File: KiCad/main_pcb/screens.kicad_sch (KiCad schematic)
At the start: 16 parts, among them U4 TI TXB0104DR, U5 ILI9488, U6 TI TXB0104DR, U7 SD Card Socket, U9 TI TXB0104DR

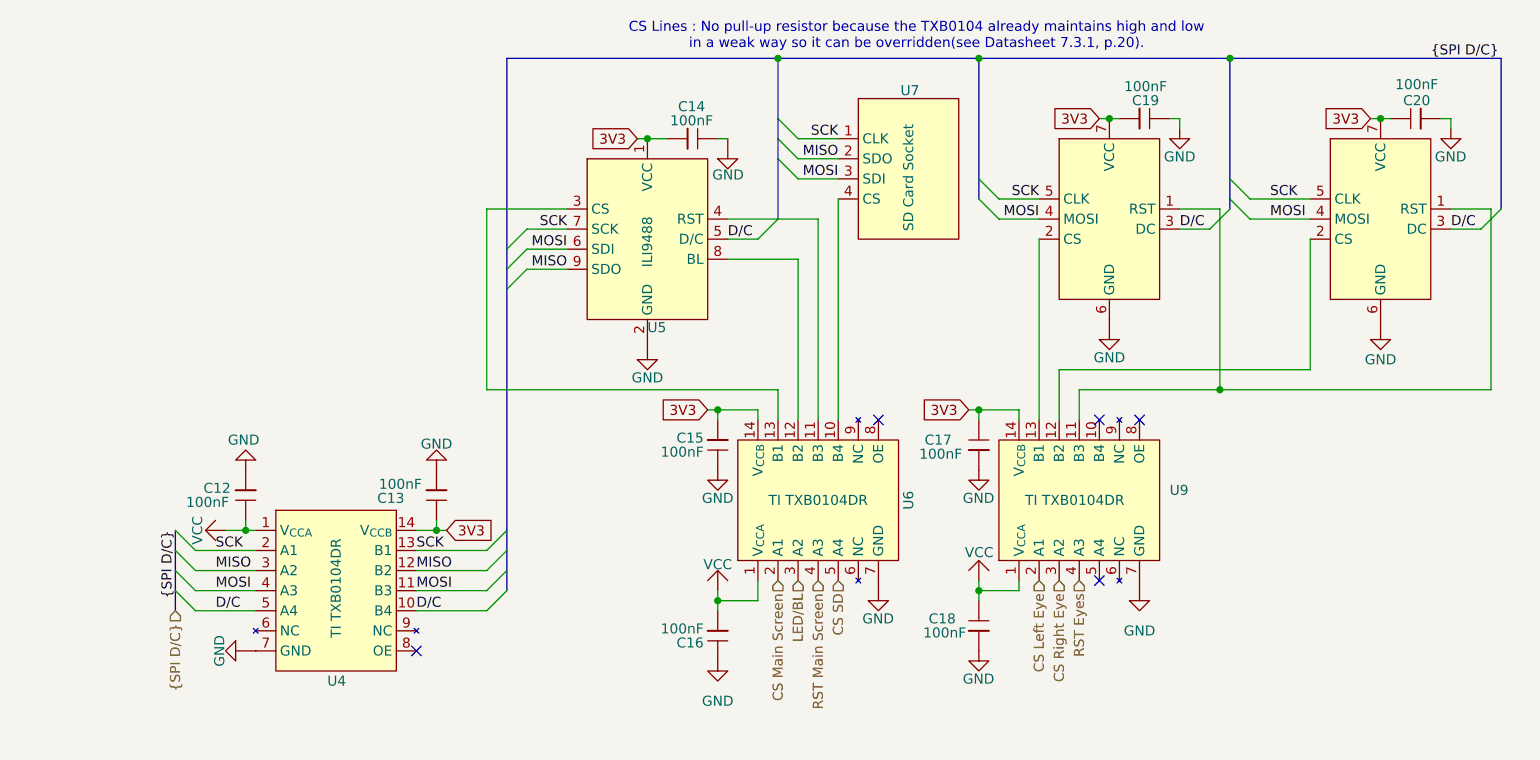
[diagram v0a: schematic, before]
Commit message: feat(schematic): Adds headers instead of direct screens plugging and refactors schematic.
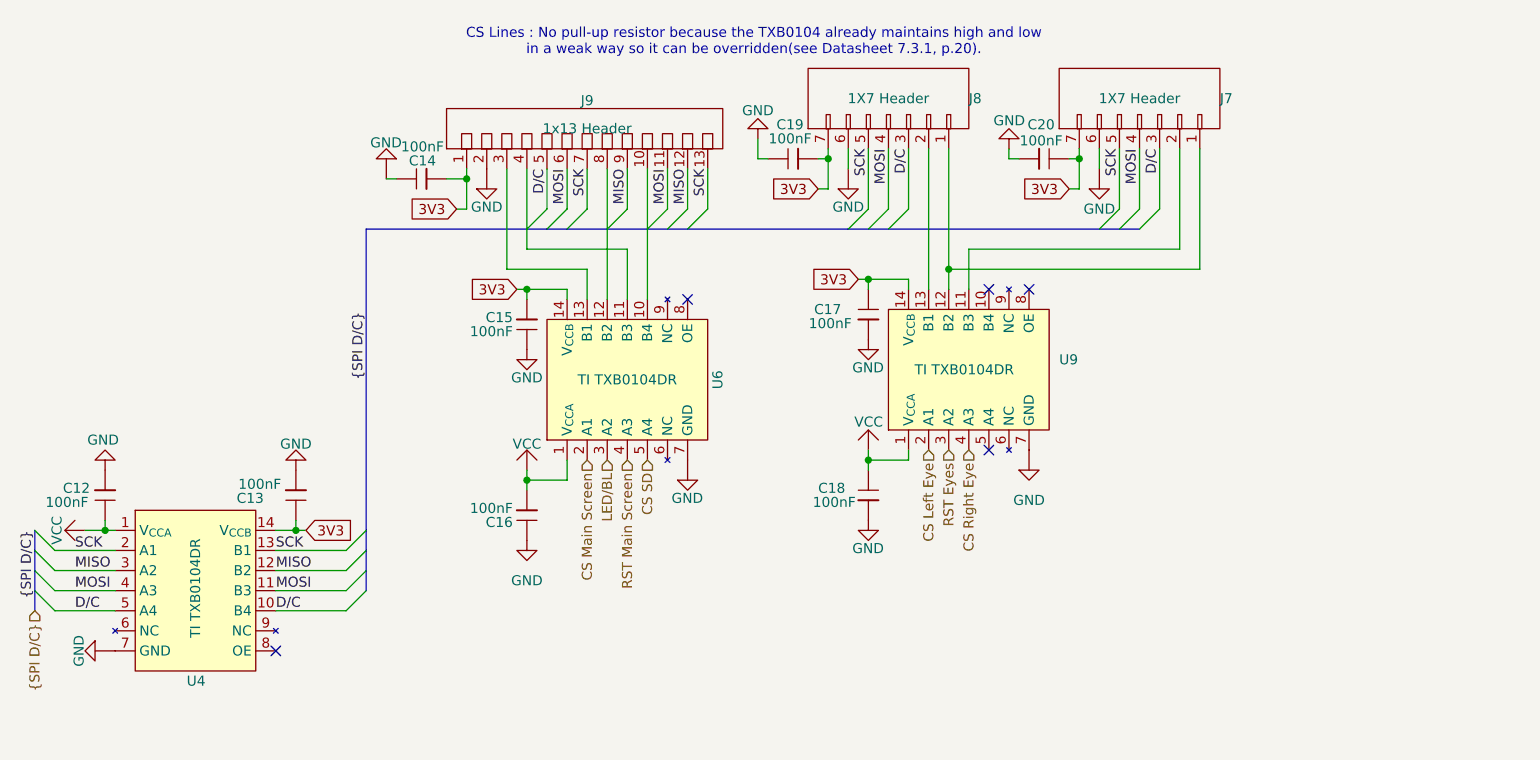
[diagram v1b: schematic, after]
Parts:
- removed U10, U8: ~, symbol Lily's Pad:GC9A01
- removed U5: ILI9488, symbol Lily's Pad:ILI9488
- removed U7: SD Card Socket, symbol Lily's Pad:SD_Card_Socket
- added J7, J8: 1X7 Header, symbol Lily's Pad:1x7_Header
- added J9: 1x13 Header, symbol Lily's Pad:1x13_Header
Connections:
- net 3V3: now also J7.7, J8.7, J9.1
- net CS Right Eye: now also U9.4 (A3); no longer U9.3 (A2)
- net D/C: now also J7.3, J8.3, J9.5
- net GND: now also J7.6, J8.6, J9.2
- net MISO: now also J9.12, J9.9
- net MOSI: now also J7.4, J8.4, J9.11, J9.6
- net RST Eyes: now also U9.3 (A2); no longer U9.4 (A3)
- net SCK: now also J7.5, J8.5, J9.13, J9.7
- net at U9.11 (B3): now also J7.2
- net at U9.12 (B2): now also J7.1, J8.1
- net at U9.13 (B1): now also J8.2
- net at U6.13 (B1): now also J9.3
- net at U6.11 (B3): now also J9.4
- net at U6.12 (B2): now also J9.8
- net at U6.10 (B4): now also J9.10
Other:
- moved on the sheet: C12, C13, C14, C15, C16, C17, C18, C19, C20, U4, U6, U9

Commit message: feat(footprints): Assigned footprints for all symbols (not all footprints are self-made)
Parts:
- J7, J8: footprint (none) -> Lilibrary:1x7 Header
- J9: footprint (none) -> Lilibrary:1x13 Header
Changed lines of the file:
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@@
 			)
 		)
-		(property "Footprint" ""
+		(property "Footprint" "Lilibrary:1x13 Header"
 			(at 93.98 59.69 0)
 			(effects
@@
 			)
 		)
-		(property "Footprint" ""
+		(property "Footprint" "Lilibrary:1x7 Header"
 			(at 132.08 55.88 0)
 			(effects
@@
 			)
 		)
-		(property "Footprint" ""
+		(property "Footprint" "Lilibrary:1x7 Header"
 			(at 163.83 55.88 0)
 			(effects

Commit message: feat(PCB): PCB first draft
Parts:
- C12, C13, C14, C15, C16, C17, C18, C19, C20: footprint Capacitor_SMD:C_0201_0603Metric_Pad0.64x0.40mm_HandSolder -> Capacitor_SMD:C_0603_1608Metric_Pad1.08x0.95mm_HandSolder
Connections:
- net CS Main Screen 3V3: now reaches J9.3, U6.13 (B1)
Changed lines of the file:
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@@
+		)
+	)
+	(label "CS Main Screen 3V3"
+		(at 83.82 76.2 180)
+		(effects
+			(font
+				(size 1.27 1.27)
+			)
+			(justify right bottom)
 		)
 	)
@@
 			)
 		)
-		(property "Footprint" "Capacitor_SMD:C_0201_0603Metric_Pad0.64x0.40mm_HandSolder"
+		(property "Footprint" "Capacitor_SMD:C_0603_1608Metric_Pad1.08x0.95mm_HandSolder"
 			(at 129.54 82.55 0)
 			(effects
@@
 			)
 		)
-		(property "Footprint" "Capacitor_SMD:C_0201_0603Metric_Pad0.64x0.40mm_HandSolder"
+		(property "Footprint" "Capacitor_SMD:C_0603_1608Metric_Pad1.08x0.95mm_HandSolder"
 			(at 57.15 106.68 0)
 			(effects
@@
 			)
 		)
-		(property "Footprint" "Capacitor_SMD:C_0201_0603Metric_Pad0.64x0.40mm_HandSolder"
+		(property "Footprint" "Capacitor_SMD:C_0603_1608Metric_Pad1.08x0.95mm_HandSolder"
 			(at 152.4 63.5 0)
 			(effects
@@
 			)
 		)
-		(property "Footprint" "Capacitor_SMD:C_0201_0603Metric_Pad0.64x0.40mm_HandSolder"
+		(property "Footprint" "Capacitor_SMD:C_0603_1608Metric_Pad1.08x0.95mm_HandSolder"
 			(at 119.38 63.5 0)
 			(effects
@@
 			)
 		)
-		(property "Footprint" "Capacitor_SMD:C_0201_0603Metric_Pad0.64x0.40mm_HandSolder"
+		(property "Footprint" "Capacitor_SMD:C_0603_1608Metric_Pad1.08x0.95mm_HandSolder"
 			(at 129.54 105.41 0)
 			(effects
@@
 			)
 		)
-		(property "Footprint" "Capacitor_SMD:C_0201_0603Metric_Pad0.64x0.40mm_HandSolder"
+		(property "Footprint" "Capacitor_SMD:C_0603_1608Metric_Pad1.08x0.95mm_HandSolder"
 			(at 86.36 85.09 0)
 			(effects
@@
 			)
 		)
-		(property "Footprint" "Capacitor_SMD:C_0201_0603Metric_Pad0.64x0.40mm_HandSolder"
+		(property "Footprint" "Capacitor_SMD:C_0603_1608Metric_Pad1.08x0.95mm_HandSolder"
 			(at 72.39 66.04 0)
 			(effects
@@
 			)
 		)
-		(property "Footprint" "Capacitor_SMD:C_0201_0603Metric_Pad0.64x0.40mm_HandSolder"
+		(property "Footprint" "Capacitor_SMD:C_0603_1608Metric_Pad1.08x0.95mm_HandSolder"
 			(at 86.36 109.22 0)
 			(effects
@@
 			)
 		)
-		(property "Footprint" "Capacitor_SMD:C_0201_0603Metric_Pad0.64x0.40mm_HandSolder"
+		(property "Footprint" "Capacitor_SMD:C_0603_1608Metric_Pad1.08x0.95mm_HandSolder"
 			(at 33.02 106.68 0)
 			(effects
